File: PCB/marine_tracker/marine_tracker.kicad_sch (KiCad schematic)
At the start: 34 parts, among them J1 Screw_Terminal_01x02, J2 Conn_ARM_JTAG_SWD_10, SW1 SW_Push, U1 STM32U575RGT6, U2 SHT40, U3 AST50147-xx, U4 MIC5504-3.3YM5, U5 SAM-M10Q, U6 25CSM04T-I/SN, Y1 32kHz768, Y3 16MHz

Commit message: add new connector for pressure sensor
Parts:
- added J3: Conn_01x06_Pin, Connector_PinHeader_2.54mm:PinHeader_1x06_P2.54mm_Vertical, symbol Connector:Conn_01x06_Pin
- added J4: BM04B-GHS-TBT, CONN_BM04B-GHS-TBT_JST, symbol BeunsLibrary:BM04B-GHS-TBT
- added R2, R3: 10k, Resistor_SMD:R_0402_1005Metric, symbol Device:R
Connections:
- net +3V3: now also J4.1, R2.1, R3.1
- net GND: now also J4.4
- net PRES_I2C2_SCL: now reaches U1.34 (PB13)
- net PRES_I2C2_SCL: now also J4.3, R2.2
- net PRES_I2C2_SDA: now reaches U1.35 (PB14)
- net PRES_I2C2_SDA: now also J4.2, R3.2
- no-connect marks 33 -> 31
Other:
- note added: "1. Antenna for satellite communication module"
- note added: "Pin Header for Pressure Sensor"
- note removed: "1. Battery connector 2. Pressure sensor connector 3. Antenna"
- moved on the sheet: C10, C13, C14, Y3

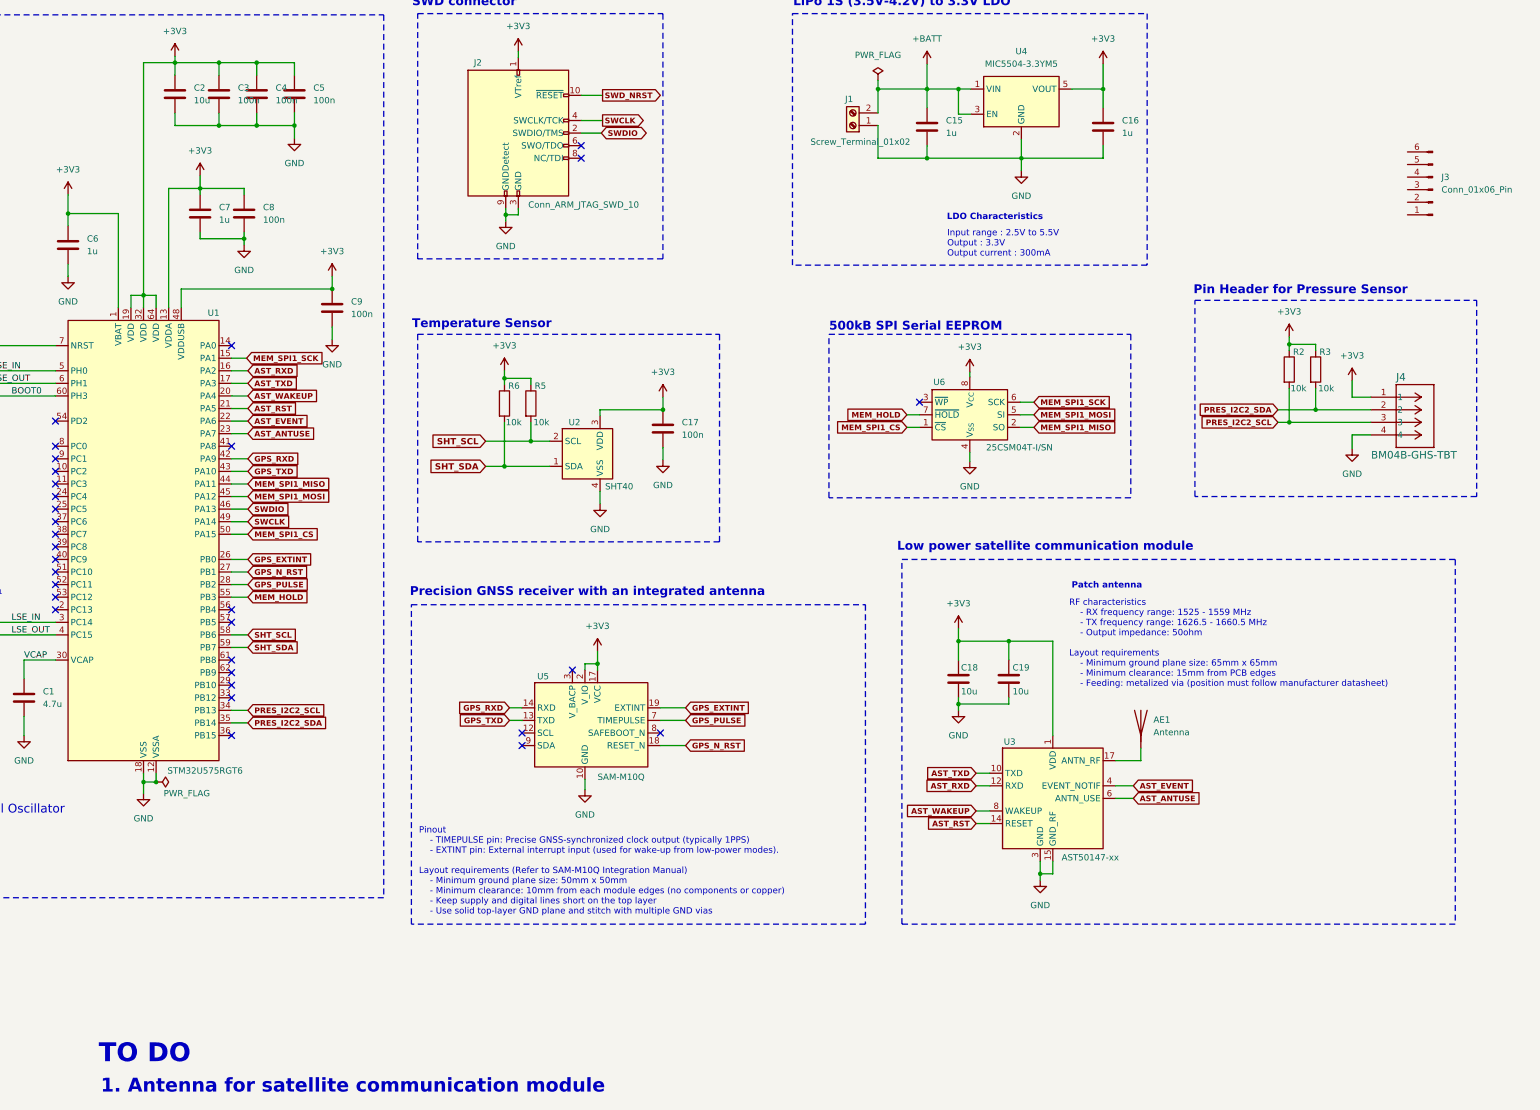
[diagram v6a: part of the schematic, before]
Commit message: add connector for satellite communication module
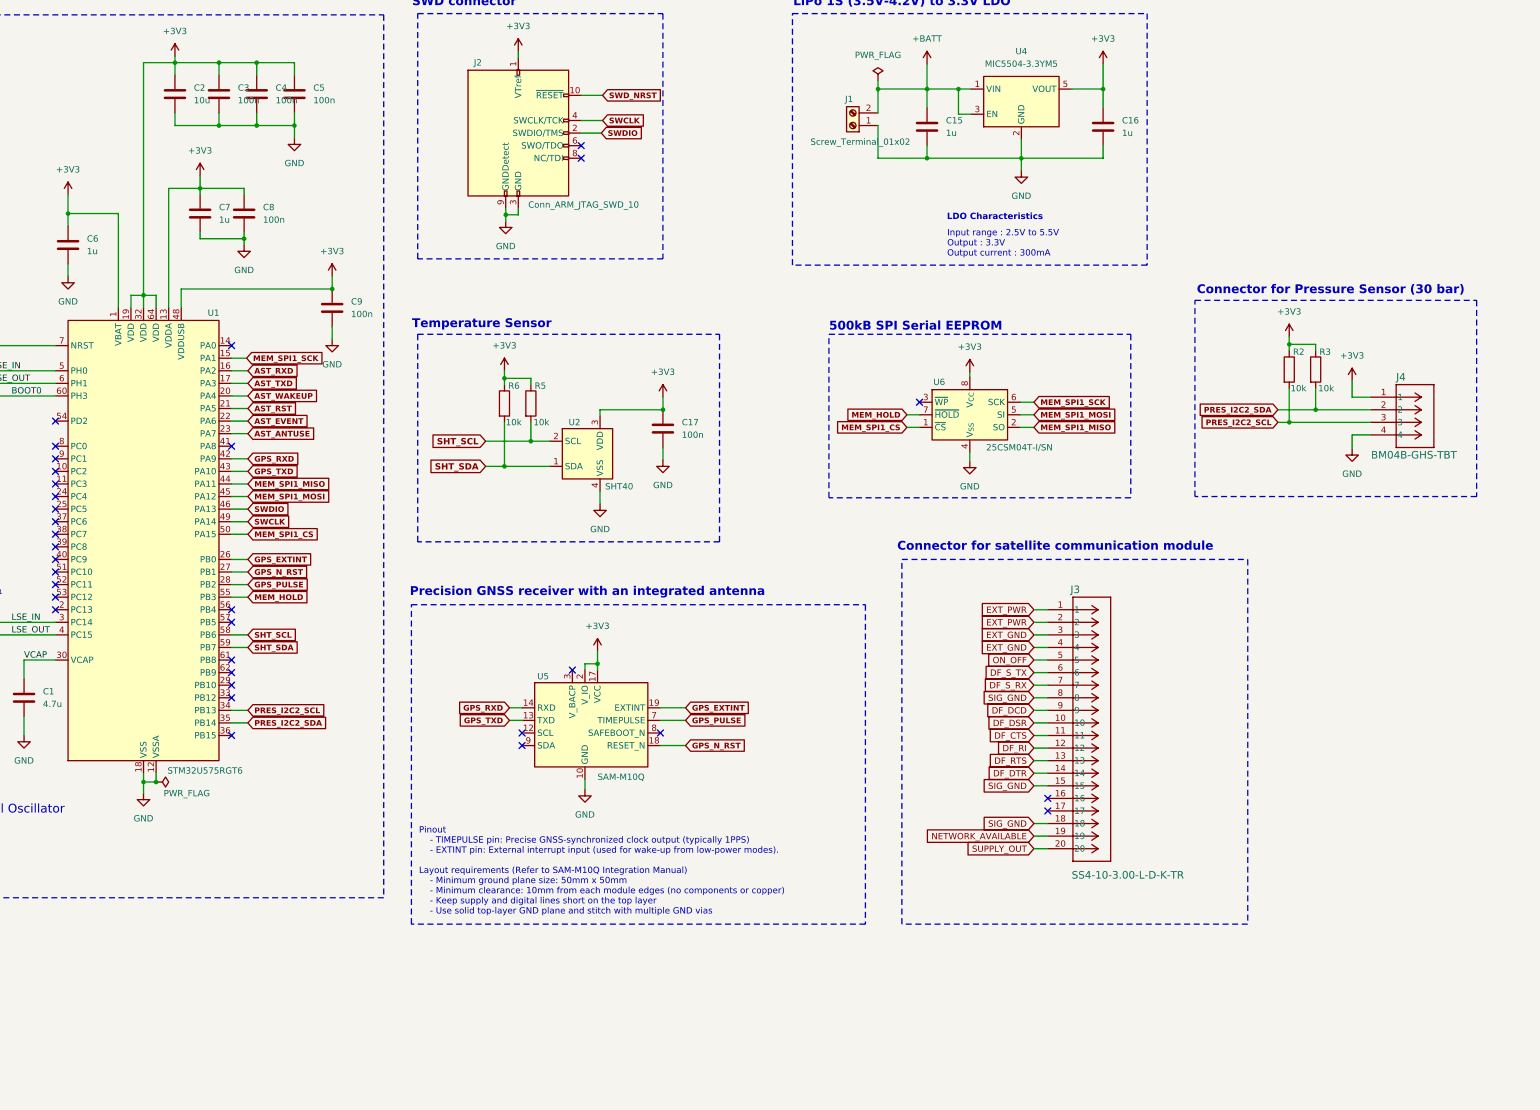
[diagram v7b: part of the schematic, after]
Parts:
- removed AE1: Antenna, symbol Device:Antenna
- removed C18, C19: 10u, Capacitor_SMD:C_0805_2012Metric, symbol Device:C
- removed J3: Conn_01x06_Pin, Connector_PinHeader_2.54mm:PinHeader_1x06_P2.54mm_Vertical, symbol Connector:Conn_01x06_Pin
- removed U3: AST50147-xx, RF_Module:Astrocast_AST50147-00, symbol RF_Module:AST50147-xx
- added J3: SS4-10-3.00-L-D-K-TR, Beuns_PCBFootprint:SAMTEC_SS4-10-3.00-L-D-TR, symbol BeunsLibrary:SS4-10-3.00-L-D-K-TR
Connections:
- new net DF_CTS: J3.11
- new net DF_DCD: J3.9
- new net DF_DSR: J3.10
- new net DF_DTR: J3.14
- new net DF_RI: J3.12
- new net DF_RTS: J3.13
- new net DF_S_RX: J3.7
- new net DF_S_TX: J3.6
- new net EXT_GND: J3.3, J3.4
- new net EXT_PWR: J3.1, J3.2
- new net NETWORK_AVAILABLE: J3.19
- new net ON_OFF: J3.5
- new net SIG_GND: J3.15, J3.18, J3.8
- new net SUPPLY_OUT: J3.20
- no-connect marks 31 -> 33
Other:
- note added: "Connector for Pressure Sensor (30 bar)"
- note added: "Connector for satellite communication module"
- note removed: "1. Antenna for satellite communication module"
- note removed: "Low power satellite communication module"
- note removed: "Patch antenna"
- note removed: "Pin Header for Pressure Sensor"
- note removed: "RF characteristics - RX frequency range: 1525 - 1559 MHz - TX frequency range: 1626.5 - 1660.5 MHz - Output impedance: 50ohm Layout requirements - Minimum ground plane size: 65mm x 65mm - Minimum clearance: 15mm from PCB edges - Feeding: metalized via (position must follow manufacturer datasheet)"
- note removed: "TO DO"

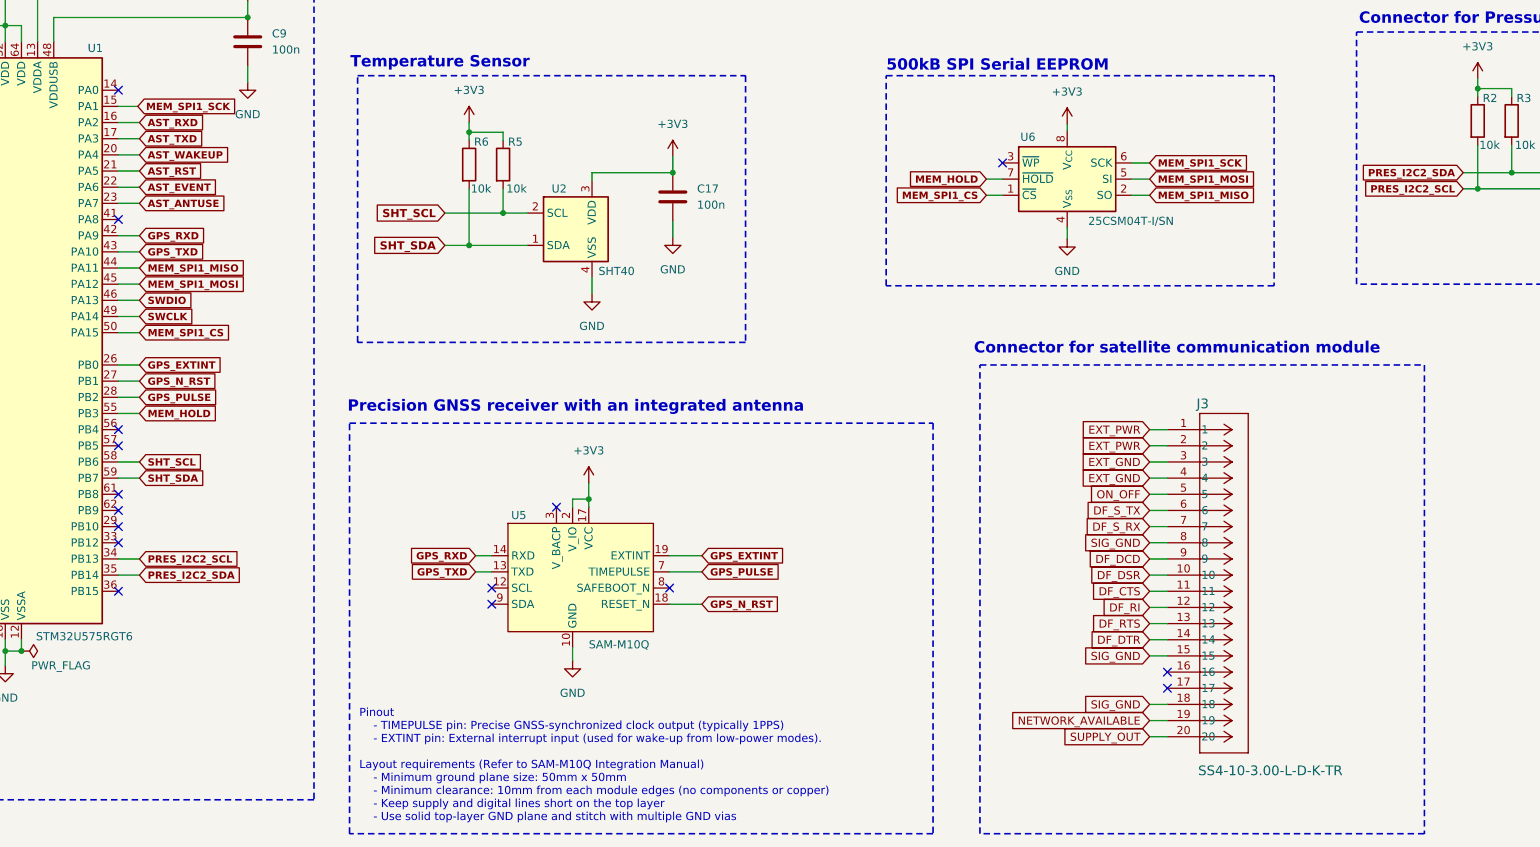
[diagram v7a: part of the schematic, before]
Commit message: add 3D models
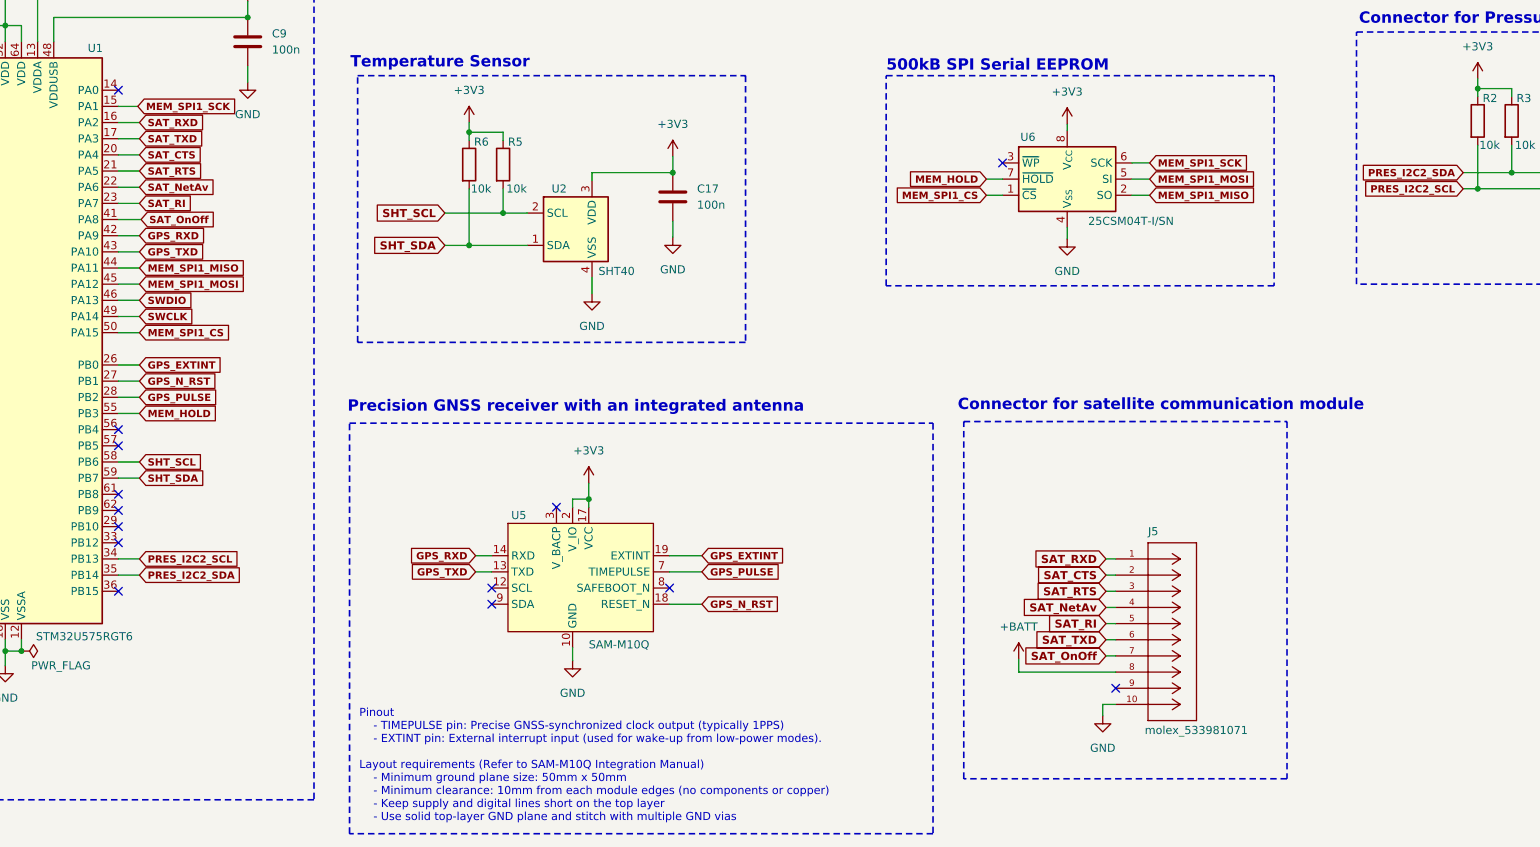
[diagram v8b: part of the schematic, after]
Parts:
- removed J3: SS4-10-3.00-L-D-K-TR, Beuns_PCBFootprint:SAMTEC_SS4-10-3.00-L-D-TR, symbol BeunsLibrary:SS4-10-3.00-L-D-K-TR
- added J5: molex_533981071, Beuns_PCBFootprint:CONN10_533981071_MOL, symbol BeunsLibrary:molex_533981071
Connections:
- net +BATT: now also J5.8
- net GND: now also J5.10
- net SAT_OnOff: now reaches U1.41 (PA8)
- net SAT_OnOff: now also J5.7
- net AST_ANTUSE renamed SAT_RI
- net SAT_RI: now also J5.5
- net AST_EVENT renamed SAT_NetAv
- net SAT_NetAv: now also J5.4
- net AST_RST renamed SAT_RTS
- net SAT_RTS: now also J5.3
- net AST_RXD renamed SAT_RXD
- net SAT_RXD: now also J5.1
- net AST_TXD renamed SAT_TXD
- net SAT_TXD: now also J5.6
- net AST_WAKEUP renamed SAT_CTS
- net SAT_CTS: now also J5.2
- no-connect marks 33 -> 31
